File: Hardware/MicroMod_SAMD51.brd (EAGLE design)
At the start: 22 x 22 mm, 30 parts, among them J2 MICROMOD-2222, U1 W25QXX6X5, U2 ATSAMD51J20A-A, Y1 32.768kHz

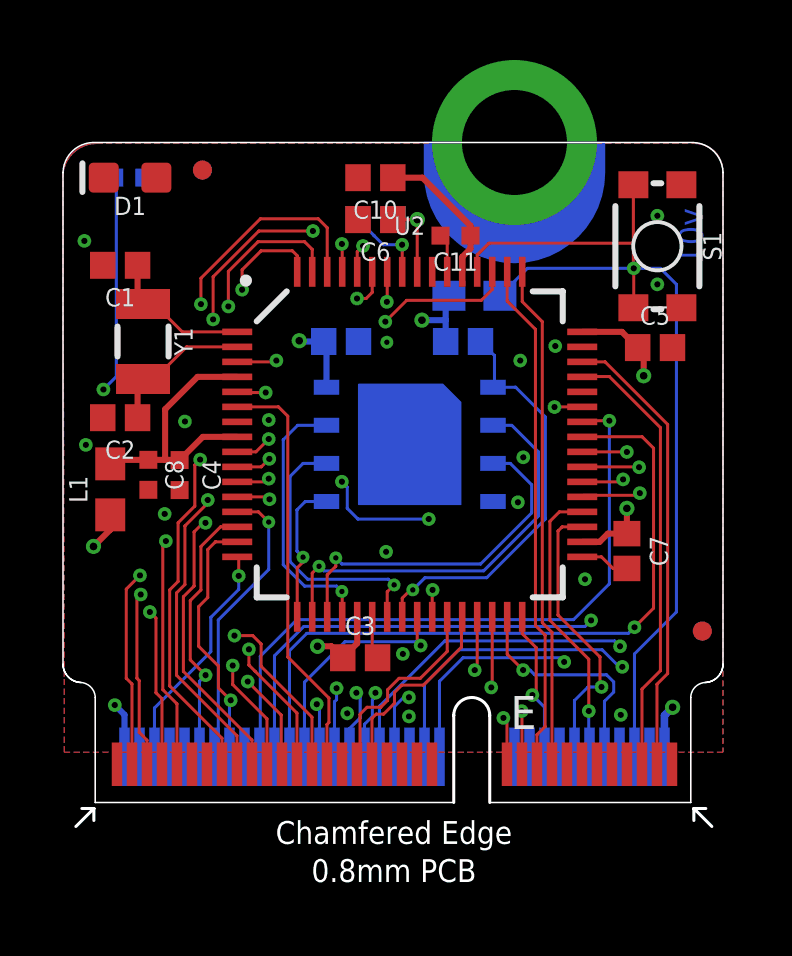
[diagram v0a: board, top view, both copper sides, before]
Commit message: Cleans up trace routing
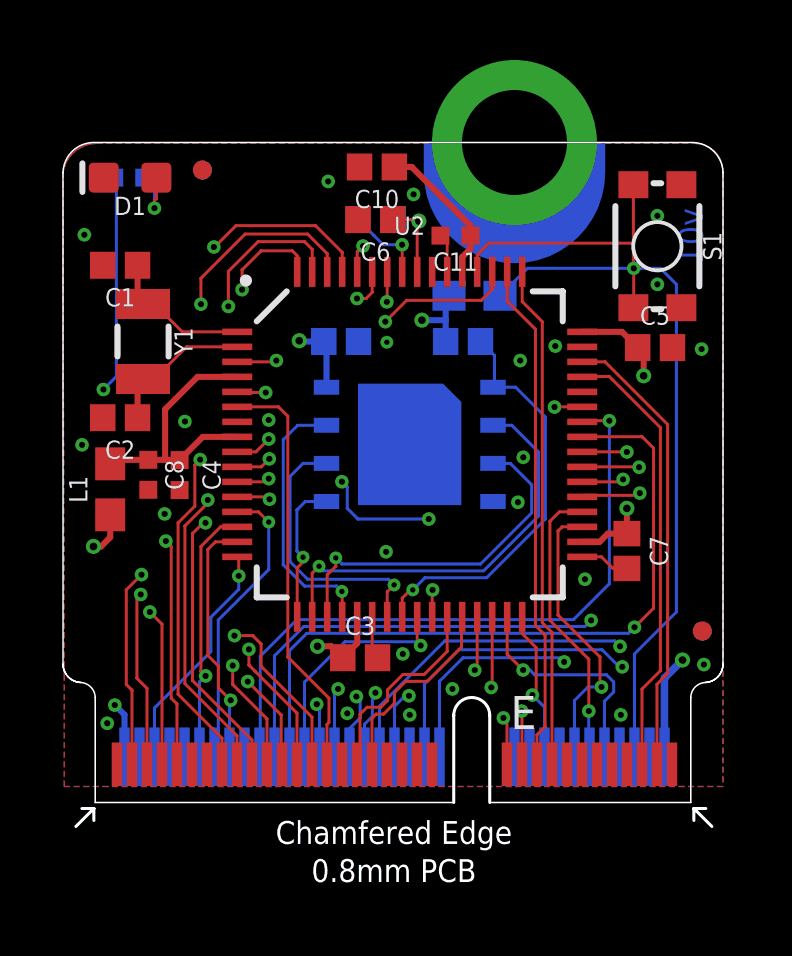
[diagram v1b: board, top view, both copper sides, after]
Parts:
- moved C10 0.36 mm to (10.5, 21.2)
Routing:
- net 3.3V: track 20.3 -> 23.1 mm
- net N$1: track 0.00 -> 2.20 mm, vias 0 -> 1
- net MISO1: track 24.0 -> 22.8 mm
- net RXI: track 17.6 -> 17.0 mm
- net MOSI1: track 23.6 -> 24.0 mm, vias 4 -> 2
- net GND: vias 15 -> 21

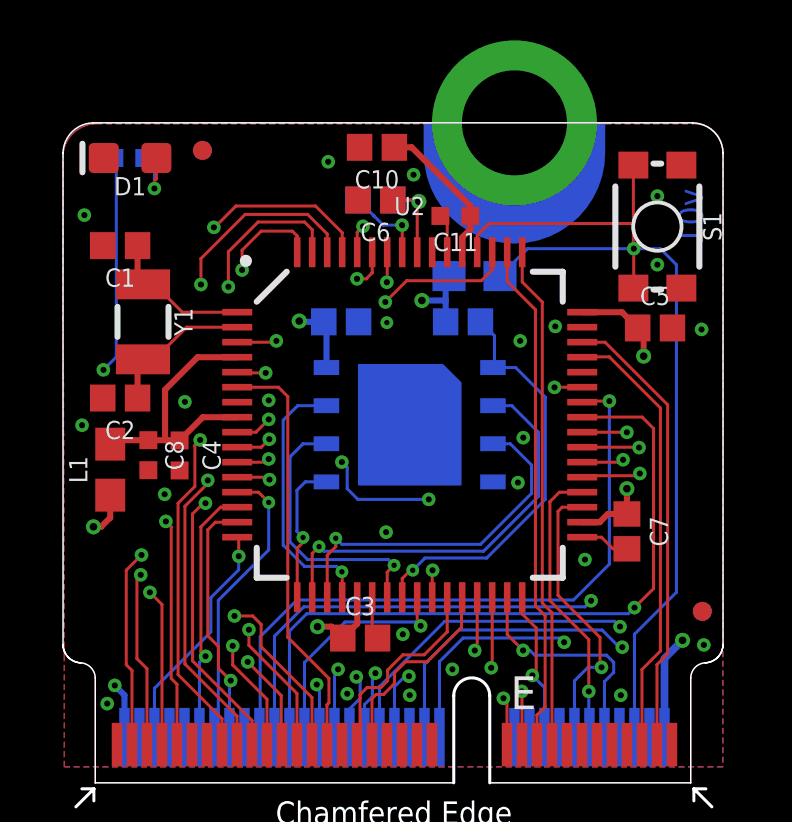
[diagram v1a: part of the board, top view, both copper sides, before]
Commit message: Adds silk, cleans up schematic
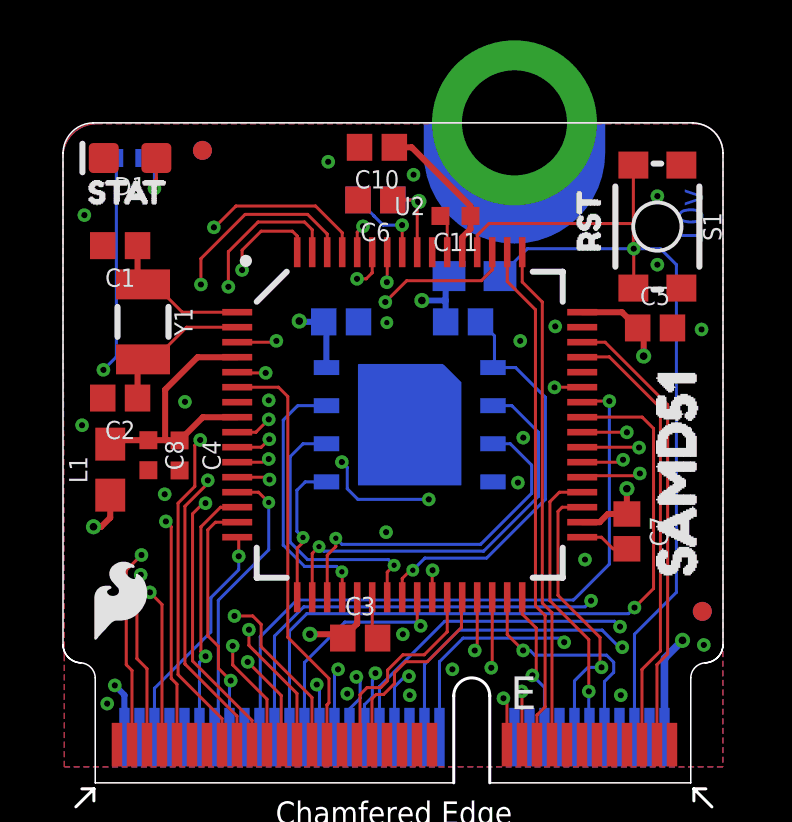
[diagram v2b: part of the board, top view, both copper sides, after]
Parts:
- added U$4: (no value), Board Label:MICROMOD1
- added U$5, U$6: (no value), Board Label:SAMD510
- added U$7: (no value), SparkFun-Aesthetics:SFE_LOGO_FLAME_.1
- added U$8: (no value), stat:STAT0
- added U$9: (no value), reset:RST0
- moved LOGO2 10.4 mm to (1.85, 5.59)
- moved LOGO6 1.30 mm to (11.8, 16.6)
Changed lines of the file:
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@@
 <setting verticaltext="up"/>
 </settings>
-<grid distance="0.01" unitdist="inch" unit="inch" style="lines" multiple="1" display="yes" altdistance="0.001" altunitdist="inch" altunit="inch"/>
+<grid distance="0.05" unitdist="inch" unit="inch" style="lines" multiple="1" display="yes" altdistance="0.005" altunitdist="inch" altunit="inch"/>
 <layers>
 <layer number="1" name="Top" color="4" fill="1" visible="yes" active="yes"/>
-<layer number="2" name="PWR_HORIZ" color="1" fill="3" visible="no" active="yes"/>
-<layer number="15" name="GND-VERT" color="4" fill="6" visible="no" active="yes"/>
+<layer number="2" name="PWR_HORIZ" color="1" fill="3" visible="yes" active="yes"/>
+<layer number="15" name="GND-VERT" color="4" fill="6" visible="yes" active="yes"/>
 <layer number="16" name="Bottom" color="3" fill="1" visible="yes" active="yes"/>
 <layer number="17" name="Pads" color="26" fill="1" visible="yes" active="yes"/>
@@
 <element name="FD7" library="SparkFun-Aesthetics" package="FIDUCIAL-MICRO" value="FIDUCIALUFIDUCIAL" x="21.3106" y="5.715" smashed="yes" rot="MR0"/>
 <element name="FD8" library="SparkFun-Aesthetics" package="FIDUCIAL-MICRO" value="FIDUCIALUFIDUCIAL" x="21.3106" y="5.715" smashed="yes"/>
-<element name="LOGO2" library="SparkFun-Aesthetics" package="OSHW-LOGO-MINI" value="OSHW-LOGOMINI" x="11.2522" y="10.033" smashed="yes" rot="MR0"/>
+<element name="LOGO2" library="SparkFun-Aesthetics" package="OSHW-LOGO-MINI" value="OSHW-LOGOMINI" x="1.8542" y="5.588" smashed="yes" rot="MR0"/>
 <element name="LOGO5" library="SparkFun-Aesthetics" package="ORDERING_INSTRUCTIONS" value="SPECIAL_INSTRUCTIONS-ORDERING" x="30.48" y="50.8" smashed="yes"/>
-<element name="LOGO6" library="SparkFun-Aesthetics" package="SFE_LOGO_NAME_FLAME_.1" value="SFE_LOGO_NAME_FLAME.1_INCH" x="11.5062" y="15.367" smashed="yes" rot="MR0"/>
+<element name="LOGO6" library="SparkFun-Aesthetics" package="SFE_LOGO_NAME_FLAME_.1" value="SFE_LOGO_NAME_FLAME.1_INCH" x="11.7602" y="16.637" smashed="yes" rot="MR0"/>
 <element name="FRAME2" library="SparkFun-Aesthetics" package="CREATIVE_COMMONS" value="FRAME-LEDGER" x="-7.62" y="-13.97" smashed="yes">
 <attribute name="DESIGNER" value="" x="-7.62" y="-13.97" size="1.778" layer="27" font="vector" ratio="15" display="off"/>
@@
 <attribute name="VALUE" x="18.288" y="18.542" size="0.6096" layer="27" font="vector" ratio="20" rot="R270" align="top-center"/>
 </element>
+<element name="U$4" library="Board Label" package="MICROMOD1" value="" x="16.637" y="7.112" smashed="yes" rot="MR0"/>
+<element name="U$5" library="Board Label" package="SAMD510" value="" x="15.875" y="5.207" smashed="yes" rot="MR0"/>
+<element name="U$6" library="Board Label" package="SAMD510" value="" x="20.447" y="5.715" smashed="yes" rot="R90"/>
+<element name="U$7" library="SparkFun-Aesthetics" package="SFE_LOGO_FLAME_.1" value="" x="1.905" y="6.096" smashed="yes"/>
+<element name="U$8" library="stat" package="STAT0" value="" x="0.127" y="19.685" smashed="yes"/>
+<element name="U$9" library="reset" package="RST0" value="" x="17.526" y="17.018" smashed="yes" rot="R90"/>
 </elements>
 <signals>
@@
 <wire x1="1.7256" y1="3.248" x2="2.049" y2="2.9246" width="0.2032" layer="16"/>
 <wire x1="2.049" y1="2.9246" x2="2.049" y2="1.525" width="0.2032" layer="16"/>
-<wire x1="9.326" y1="4.826" x2="8.945" y2="5.207" width="0.2032" layer="1"/>
-<wire x1="8.945" y1="5.207" x2="8.4836" y2="5.207" width="0.2032" layer="1"/>
-<via x="8.4836" y="5.207" extent="1-16" drill="0.254"/>
+<wire x1="9.326" y1="4.826" x2="9.199" y2="4.953" width="0.2032" layer="1"/>
+<wire x1="9.199" y1="4.953" x2="8.2296" y2="4.953" width="0.2032" layer="1"/>
+<via x="8.2296" y="4.953" extent="1-16" drill="0.254"/>
 <wire x1="1.5748" y1="9.5894" x2="1.5748" y2="8.84" width="0.2032" layer="1"/>
 <wire x1="1.5748" y1="8.84" x2="1.27" y2="8.5352" width="0.2032" layer="1"/>
@@
 <via x="5.6568" y="4.5662" extent="1-16" drill="0.2032"/>
 <wire x1="13.648" y1="4.4876" x2="13.7242" y2="4.4114" width="0.1016" layer="2"/>
-<wire x1="13.648" y1="4.4876" x2="6.0656" y2="4.4876" width="0.1016" layer="2"/>
-<wire x1="6.0656" y1="4.4876" x2="5.987" y2="4.5662" width="0.1016" layer="2"/>
-<wire x1="5.6568" y1="4.5662" x2="5.987" y2="4.5662" width="0.1016" layer="2"/>
+<wire x1="13.648" y1="4.4876" x2="5.7354" y2="4.4876" width="0.1016" layer="2"/>
+<wire x1="5.6568" y1="4.5662" x2="5.7354" y2="4.4876" width="0.1016" layer="2"/>
 <wire x1="6.799" y1="2.789" x2="5.6568" y2="3.9312" width="0.1016" layer="1"/>
 <wire x1="5.6568" y1="4.5662" x2="5.6568" y2="3.9312" width="0.1016" layer="1"/>

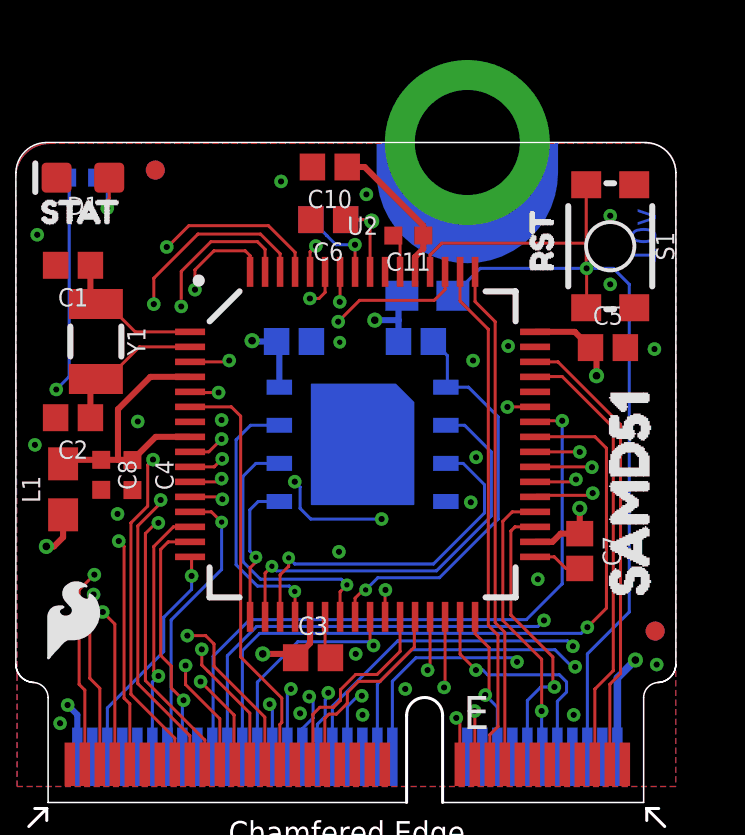
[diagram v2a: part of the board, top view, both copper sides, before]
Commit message: Removes reset button
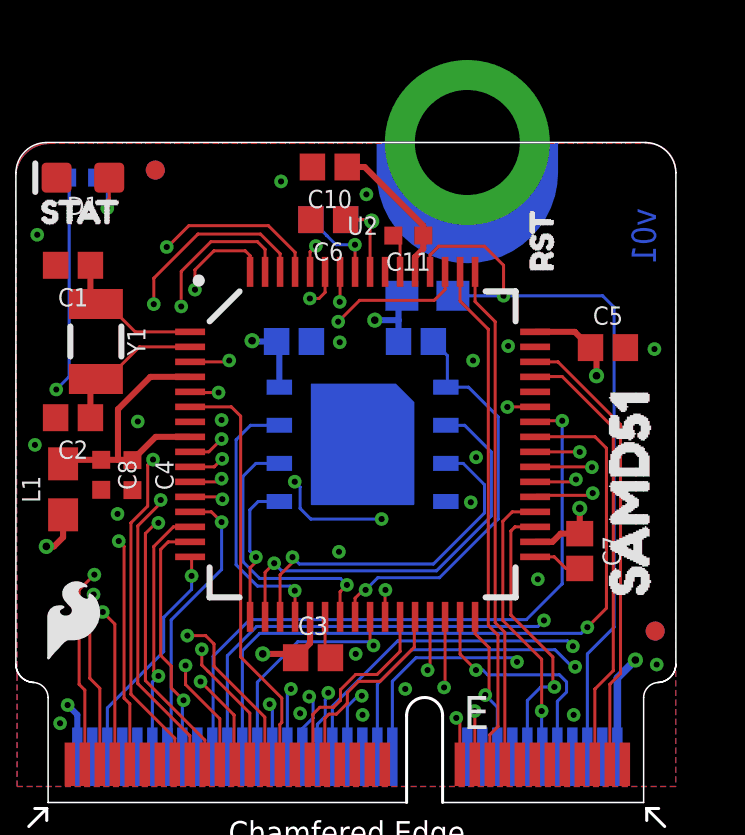
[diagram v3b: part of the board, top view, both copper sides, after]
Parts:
- removed S1: MOMENTARY-SWITCH-SPST-SMD-4.6X2.8MM, SparkFun-Switches:TACTILE_SWITCH_SMD_4.6X2.8MM
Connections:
- net !RESET: no longer S1.1, S1.2
- net GND: no longer S1.3, S1.4
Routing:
- net !RESET: track 32.8 -> 25.3 mm
- net GND: vias 21 -> 19

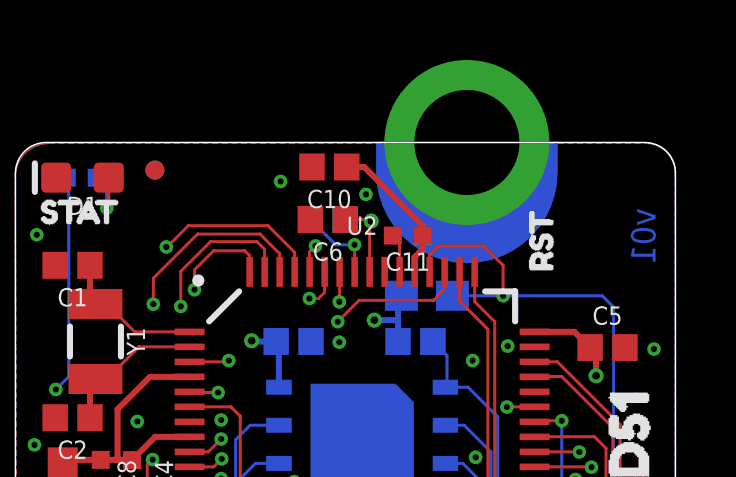
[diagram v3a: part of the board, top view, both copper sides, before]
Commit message: Updates processor board with new screw design
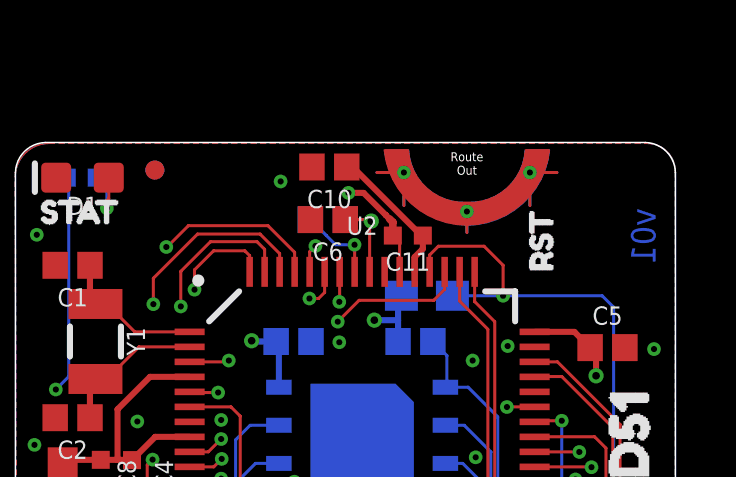
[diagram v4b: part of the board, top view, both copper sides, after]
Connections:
- net GND: now also J2.GND1, J2.GND2, J2.GND3; no longer J2.GND, J2.GND-SM-B
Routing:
- net GND: track 4.39 -> 6.72 mm
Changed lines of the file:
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@@
 <layers>
 <layer number="1" name="Top" color="4" fill="1" visible="yes" active="yes"/>
-<layer number="2" name="PWR_HORIZ" color="1" fill="3" visible="yes" active="yes"/>
-<layer number="15" name="GND-VERT" color="4" fill="6" visible="yes" active="yes"/>
+<layer number="2" name="PWR_HORIZ" color="1" fill="3" visible="no" active="yes"/>
+<layer number="15" name="GND-VERT" color="4" fill="6" visible="no" active="yes"/>
 <layer number="16" name="Bottom" color="3" fill="1" visible="yes" active="yes"/>
 <layer number="17" name="Pads" color="26" fill="1" visible="yes" active="yes"/>
@@
 </polygon>
 <contactref element="J2" pad="33"/>
-<contactref element="J2" pad="GND-SM-B"/>
+<contactref element="J2" pad="GND2"/>
 <contactref element="J2" pad="7"/>
 <contactref element="J2" pad="75"/>
-<contactref element="J2" pad="GND"/>
+<contactref element="J2" pad="GND1"/>
 <contactref element="J2" pad="39"/>
 <contactref element="J2" pad="1"/>
@@
 <via x="8.8398" y="20.7022" extent="1-16" drill="0.2032"/>
 <via x="21.2858" y="15.1142" extent="1-16" drill="0.2032"/>
-<via x="11.6846" y="20.2704" extent="1-16" drill="0.2032"/>
+<via x="11.1004" y="20.3212" extent="1-16" drill="0.2032"/>
 <via x="12.9794" y="3.7846" extent="1-16" drill="0.2032"/>
 <via x="1.4732" y="2.6416" extent="1-16" drill="0.2032"/>
 <via x="21.3614" y="4.5974" extent="1-16" drill="0.2032"/>
+<contactref element="J2" pad="GND3"/>
+<wire x1="12.581" y1="18.8968" x2="12.581" y2="19.3431" width="0.254" layer="1"/>
+<wire x1="12.581" y1="19.3431" x2="12.46955" y2="19.45455" width="0.254" layer="1"/>
+<wire x1="12.46955" y1="19.45455" x2="12.3444" y2="19.5797" width="0.2032" layer="1"/>
+<wire x1="12.3444" y1="19.5797" x2="12.3444" y2="19.5801" width="0.2032" layer="1"/>
+<wire x1="12.3444" y1="19.5801" x2="11.6033" y2="20.3212" width="0.2032" layer="1"/>
+<wire x1="11.6033" y1="20.3212" x2="11.1004" y2="20.3212" width="0.2032" layer="1"/>
 </signal>
 <signal name="D3">
@@
 <contactref element="C10" pad="1"/>
 <contactref element="C11" pad="1"/>
-<wire x1="13.581" y1="18.8968" x2="13.581" y2="19.227" width="0.2032" layer="1"/>
-<wire x1="13.581" y1="19.227" x2="11.6244" y2="21.1836" width="0.2032" layer="1"/>
-<wire x1="11.6244" y1="21.1836" x2="11.0448" y2="21.1836" width="0.2032" layer="1"/>
+<wire x1="13.581" y1="18.8968" x2="13.5302" y2="18.8968" width="0.2032" layer="1"/>
+<wire x1="13.5302" y1="18.8968" x2="11.2434" y2="21.1836" width="0.2032" layer="1"/>
+<wire x1="11.2434" y1="21.1836" x2="11.0448" y2="21.1836" width="0.2032" layer="1"/>
 <wire x1="13.307" y1="17.688" x2="13.307" y2="18.183" width="0.2032" layer="1"/>
 <wire x1="13.581" y1="18.457" x2="13.581" y2="18.8968" width="0.2032" layer="1"/>
